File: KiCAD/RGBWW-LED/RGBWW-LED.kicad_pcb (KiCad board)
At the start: 2 copper layers, 0 parts

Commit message: added some library components and edited pdf
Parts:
- added C1: 1u, Capacitor_SMD:C_0603_1608Metric, F.Cu at (58.0, 82.9)
- added C10: 1u, Capacitor_SMD:C_0603_1608Metric, F.Cu at (58.0, 63.3)
- added C2: 1u, Capacitor_SMD:C_0603_1608Metric, F.Cu at (58.0, 85.4)
- added C3: 1u, Capacitor_SMD:C_0603_1608Metric, F.Cu at (90.6, 60.8)
- added C4: 1u, Capacitor_SMD:C_0603_1608Metric, F.Cu at (90.6, 63.3)
- added C5: 1u, Capacitor_SMD:C_0603_1608Metric, F.Cu at (90.6, 38.8)
- added C6: 1u, Capacitor_SMD:C_0603_1608Metric, F.Cu at (90.6, 41.3)
- added C7: 1u, Capacitor_SMD:C_0603_1608Metric, F.Cu at (58.0, 38.8)
- added C8: 1u, Capacitor_SMD:C_0603_1608Metric, F.Cu at (58.0, 41.3)
- added C9: 1u, Capacitor_SMD:C_0603_1608Metric, F.Cu at (58.0, 60.8)
- added J1: Conn_01x04, Connector_PinHeader_2.54mm:PinHeader_1x04_P2.54mm_Horizontal, F.Cu at (90.9, 84.0)
- added J2: Conn_01x04, Connector_PinHeader_2.54mm:PinHeader_1x04_P2.54mm_Horizontal, F.Cu at (90.9, 96.2)
- added R1: 4k7, Resistor_SMD:R_0603_1608Metric, F.Cu at (58.0, 87.9)
- added R10: 0R, Resistor_SMD:R_0603_1608Metric, F.Cu at (90.6, 73.4)
- added R11: 0R, Resistor_SMD:R_0603_1608Metric, F.Cu at (90.6, 75.9)
- added R12: 4k7, Resistor_SMD:R_0603_1608Metric, F.Cu at (90.6, 78.4)
- added R13: 0R, Resistor_SMD:R_0603_1608Metric, F.Cu at (90.6, 43.8)
- added R14: 0R, Resistor_SMD:R_0603_1608Metric, F.Cu at (90.6, 46.3)
- added R15: 0R, Resistor_SMD:R_0603_1608Metric, F.Cu at (90.6, 48.8)
- added R16: 0R, Resistor_SMD:R_0603_1608Metric, F.Cu at (90.6, 51.3)
- added R17: 0R, Resistor_SMD:R_0603_1608Metric, F.Cu at (90.6, 53.8)
- added R18: 4k7, Resistor_SMD:R_0603_1608Metric, F.Cu at (90.6, 56.3)
- added R19: 0R, Resistor_SMD:R_0603_1608Metric, F.Cu at (58.0, 43.8)
- added R2: 0R, Resistor_SMD:R_0603_1608Metric, F.Cu at (58.0, 90.4)
- added R20: 0R, Resistor_SMD:R_0603_1608Metric, F.Cu at (58.0, 46.3)
- added R21: 0R, Resistor_SMD:R_0603_1608Metric, F.Cu at (58.0, 48.8)
- added R22: 0R, Resistor_SMD:R_0603_1608Metric, F.Cu at (58.0, 51.3)
- added R23: 0R, Resistor_SMD:R_0603_1608Metric, F.Cu at (58.0, 53.8)
- added R24: 4k7, Resistor_SMD:R_0603_1608Metric, F.Cu at (58.0, 56.3)
- added R25: 0R, Resistor_SMD:R_0603_1608Metric, F.Cu at (58.0, 65.9)
- added R26: 0R, Resistor_SMD:R_0603_1608Metric, F.Cu at (58.0, 68.4)
- added R27: 0R, Resistor_SMD:R_0603_1608Metric, F.Cu at (58.0, 70.9)
- added R28: 0R, Resistor_SMD:R_0603_1608Metric, F.Cu at (58.0, 73.4)
- added R29: 0R, Resistor_SMD:R_0603_1608Metric, F.Cu at (58.0, 75.9)
- added R3: 0R, Resistor_SMD:R_0603_1608Metric, F.Cu at (58.0, 93.0)
- added R30: 4k7, Resistor_SMD:R_0603_1608Metric, F.Cu at (58.0, 78.4)
- added R31: 100R, Resistor_SMD:R_0603_1608Metric, F.Cu at (104.0, 82.9)
- added R32: 100R, Resistor_SMD:R_0603_1608Metric, F.Cu at (104.0, 85.4)
- added R4: 0R, Resistor_SMD:R_0603_1608Metric, F.Cu at (58.0, 95.5)
- added R5: 0R, Resistor_SMD:R_0603_1608Metric, F.Cu at (58.0, 98.0)
- added R6: 0R, Resistor_SMD:R_0603_1608Metric, F.Cu at (58.0, 100.5)
- added R7: 0R, Resistor_SMD:R_0603_1608Metric, F.Cu at (90.6, 65.9)
- added R8: 0R, Resistor_SMD:R_0603_1608Metric, F.Cu at (90.6, 68.4)
- added R9: 0R, Resistor_SMD:R_0603_1608Metric, F.Cu at (90.6, 70.9)
- added U1: H5050RGBWW-ZB-96427, LEDandDriver:LED_RGBWW_5050_10, F.Cu at (63.3, 82.4)
- added U10: H5050RGBWW-ZB-96427, LEDandDriver:LED_RGBWW_5050_10, F.Cu at (102.6, 38.2)
- added U11: H5050RGBWW-ZB-96427, LEDandDriver:LED_RGBWW_5050_10, F.Cu at (70.0, 38.2)
- added U12: WS2805, LEDandDriver:SOP-10-6mm-1mm, F.Cu at (109.2, 38.2)
- added U13: H5050RGBWW-ZB-96427, LEDandDriver:LED_RGBWW_5050_10, F.Cu at (70.0, 60.3)
- added U14: H5050RGBWW-ZB-96427, LEDandDriver:LED_RGBWW_5050_10, F.Cu at (83.3, 82.4)
- added U15: H5050RGBWW-ZB-96427, LEDandDriver:LED_RGBWW_5050_10, F.Cu at (115.9, 60.3)
- added U16: WS2805, LEDandDriver:SOP-10-6mm-1mm, F.Cu at (76.6, 38.2)
- added U17: H5050RGBWW-ZB-96427, LEDandDriver:LED_RGBWW_5050_10, F.Cu at (115.9, 38.2)
- added U18: H5050RGBWW-ZB-96427, LEDandDriver:LED_RGBWW_5050_10, F.Cu at (83.3, 38.2)
- added U19: H5050RGBWW-ZB-96427, LEDandDriver:LED_RGBWW_5050_10, F.Cu at (76.6, 60.3)
- added U2: H5050RGBWW-ZB-96427, LEDandDriver:LED_RGBWW_5050_10, F.Cu at (95.9, 60.3)
- added U20: WS2805, LEDandDriver:SOP-10-6mm-1mm, F.Cu at (83.3, 60.3)
- added U3: WS2805, LEDandDriver:SOP-10-6mm-1mm, F.Cu at (70.0, 82.4)
- added U4: H5050RGBWW-ZB-96427, LEDandDriver:LED_RGBWW_5050_10, F.Cu at (95.9, 38.2)
- added U5: H5050RGBWW-ZB-96427, LEDandDriver:LED_RGBWW_5050_10, F.Cu at (63.3, 38.2)
- added U6: H5050RGBWW-ZB-96427, LEDandDriver:LED_RGBWW_5050_10, F.Cu at (63.3, 60.3)
- added U7: H5050RGBWW-ZB-96427, LEDandDriver:LED_RGBWW_5050_10, F.Cu at (76.6, 82.4)
- added U8: WS2805, LEDandDriver:SOP-10-6mm-1mm, F.Cu at (102.6, 60.3)
- added U9: H5050RGBWW-ZB-96427, LEDandDriver:LED_RGBWW_5050_10, F.Cu at (109.2, 60.3)

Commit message: started layout, some mods to the lib
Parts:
- R10, R11, R13, R14, R15, R16, R17, R19, R2, R20, R21, R22, R23, R25, R26, R27, R28, R29, R3, R4, R5, R6, R7, R8, R9: value 0R -> 10R
- moved U12 123.5 mm to (45.1, 143.8)
- moved U3 112.2 mm to (153.1, 157.8)
- moved C2 110.4 mm to (140.8, 158.5)
- moved R1 110.4 mm to (140.8, 161.0)
- moved R2 110.4 mm to (140.8, 163.5)
- moved R3 110.4 mm to (140.8, 166.0)
- moved R4 110.4 mm to (140.8, 168.5)
- moved R5 110.4 mm to (140.8, 171.0)
- moved R6 110.4 mm to (140.8, 173.6)
- moved C1 110.4 mm to (140.8, 156.0)
- moved C8 108.7 mm to (119.5, 130.9), turned to -90 degrees
- moved C6 108.0 mm to (29.8, 130.5)
- moved R15 108.0 mm to (29.8, 138.0)
- moved R18 108.0 mm to (29.8, 145.6)
- moved C5 108.0 mm to (29.8, 128.0)
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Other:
- board outline added: 150 x 15 mm

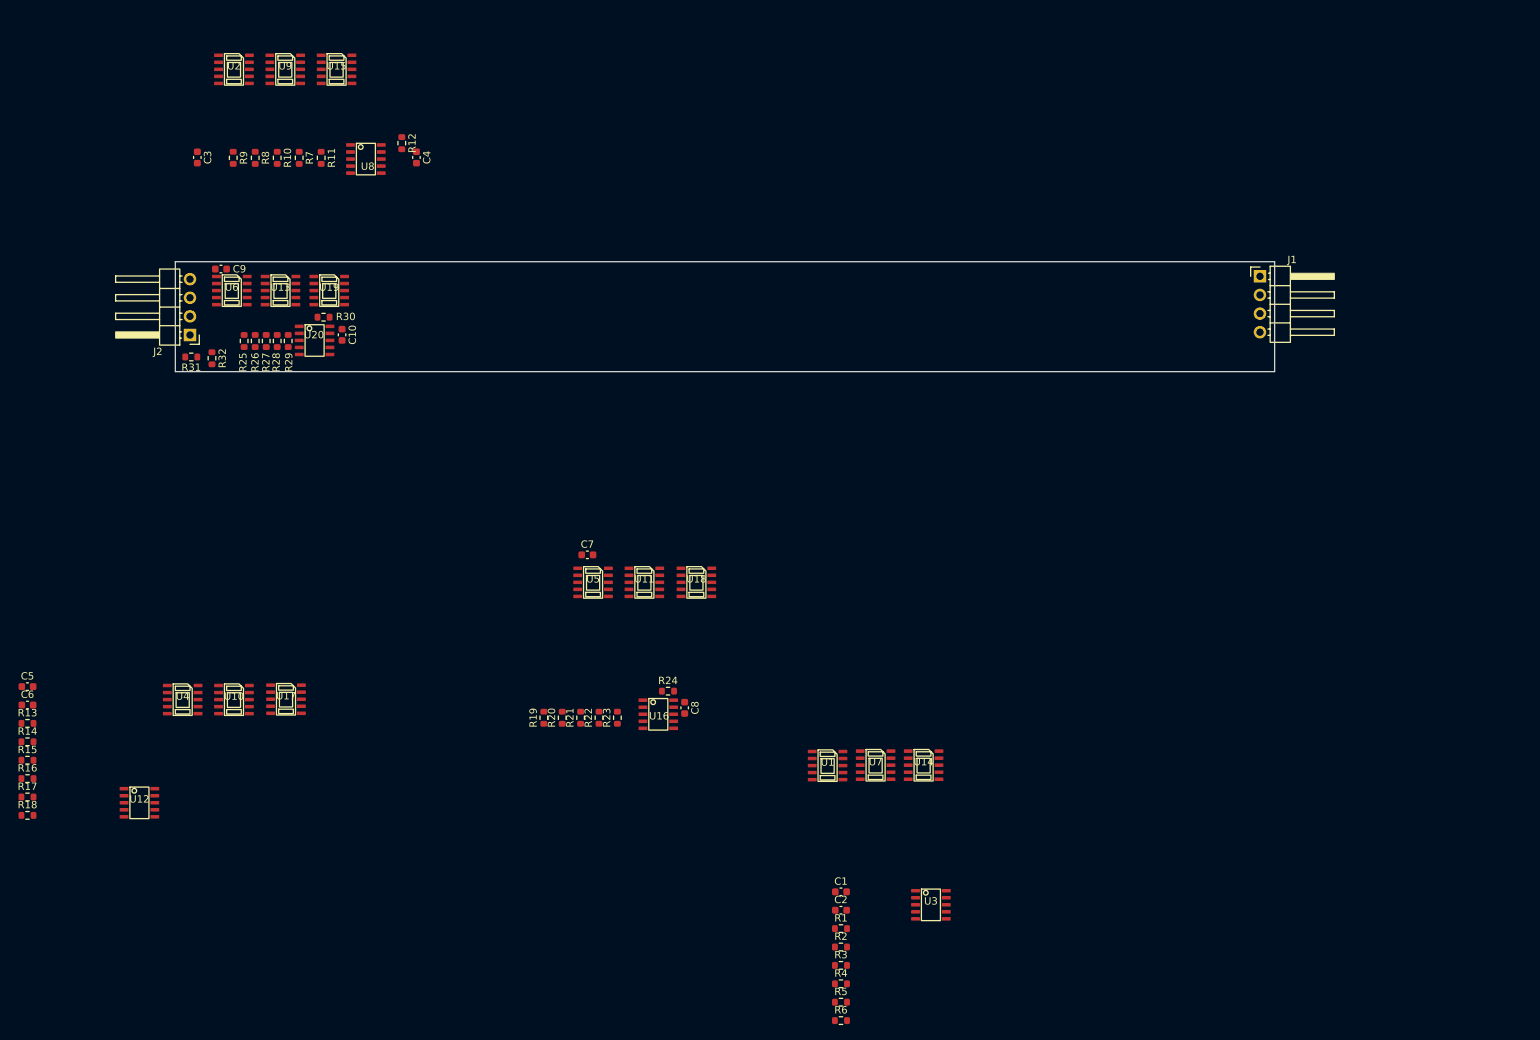
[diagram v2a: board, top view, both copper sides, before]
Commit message: added some datasheet and started controller
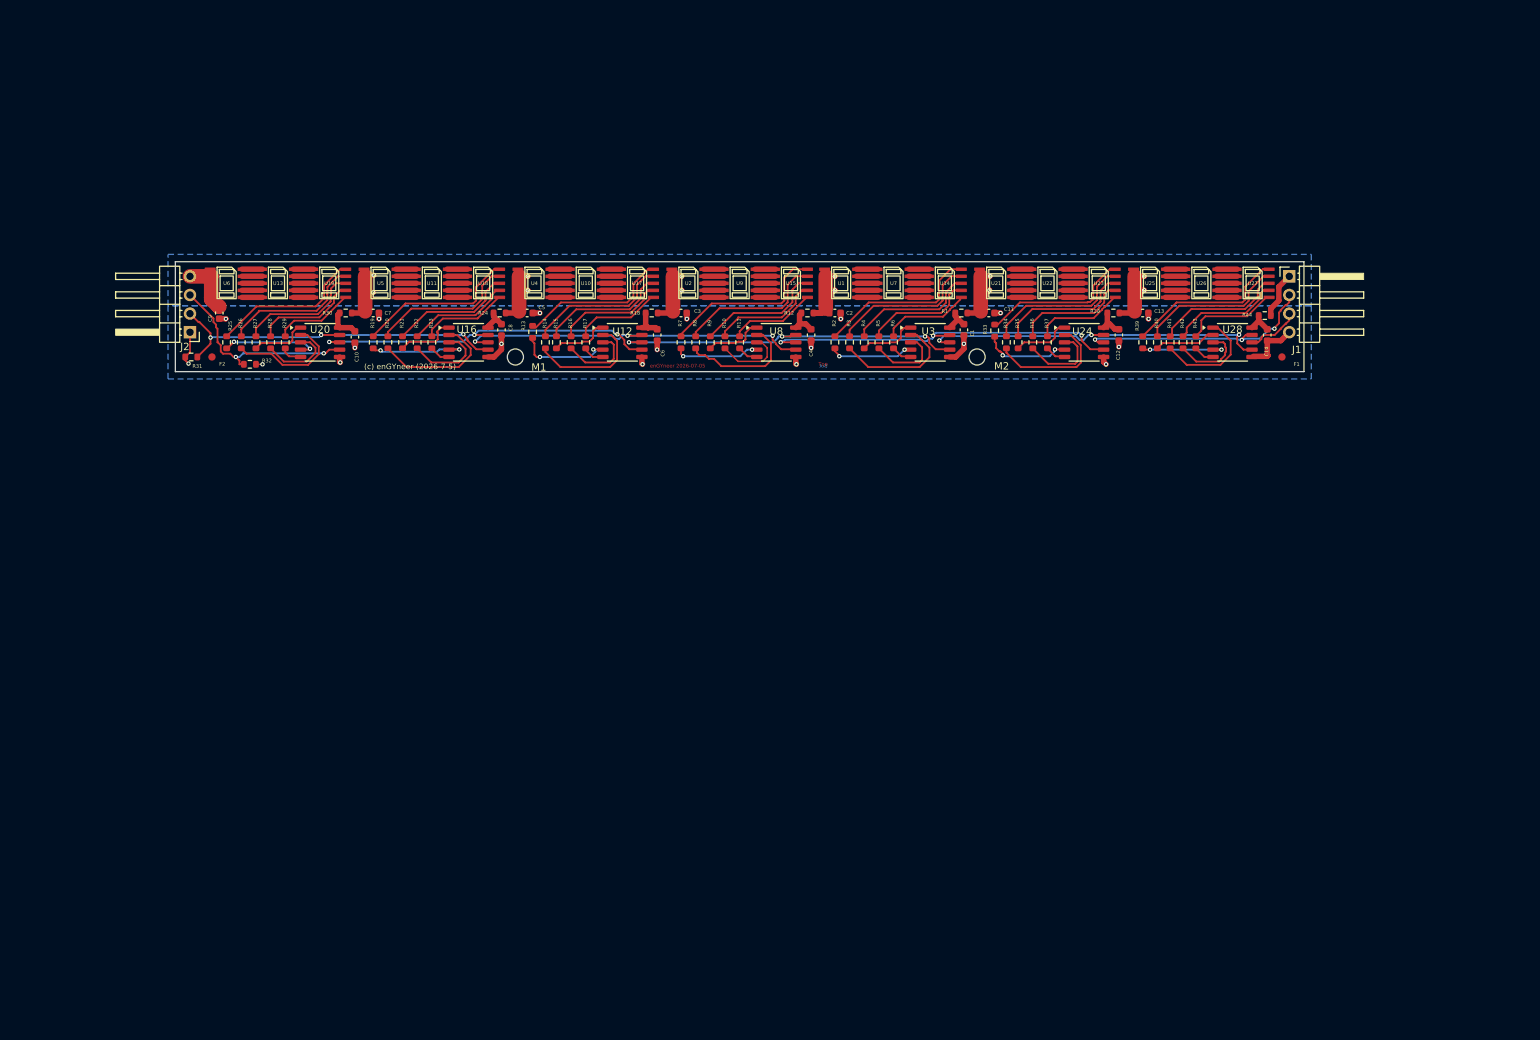
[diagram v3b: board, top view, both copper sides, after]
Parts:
- added C11: 1u, LEDandDriver:C_0603_1608Metric_LedPrj, F.Cu at (161.0, 77.0)
- added C12: 1u, LEDandDriver:C_0603_1608Metric_LedPrj, F.Cu at (178.8, 80.0)
- added C13: 1u, LEDandDriver:C_0603_1608Metric_LedPrj, F.Cu at (182.0, 77.0)
- added C14: 1u, LEDandDriver:C_0603_1608Metric_LedPrj, F.Cu at (199.0, 80.0)
- added F1: Fiducial, Fiducial:Fiducial_1mm_Mask2mm, F.Cu at (201.0, 83.0)
- added F2: Fiducial, Fiducial:Fiducial_1mm_Mask2mm, F.Cu at (55.0, 83.0)
- added M1: MountingHole, MountingHole:MountingHole_2.2mm_M2, F.Cu at (96.4, 83.0)
- added M2: MountingHole, MountingHole:MountingHole_2.2mm_M2, F.Cu at (159.4, 83.0)
- added R33: 10R, LEDandDriver:R_0603_1608Metric_LedPrj, F.Cu at (161.8, 79.4)
- added R34: 10R, LEDandDriver:R_0603_1608Metric_LedPrj, F.Cu at (163.4, 81.0)
- added R35: 10R, LEDandDriver:R_0603_1608Metric_LedPrj, F.Cu at (165.0, 81.0)
- added R36: 10R, LEDandDriver:R_0603_1608Metric_LedPrj, F.Cu at (167.0, 81.0)
- added R37: 10R, LEDandDriver:R_0603_1608Metric_LedPrj, F.Cu at (169.0, 81.0)
- added R38: 4k7, LEDandDriver:R_0603_1608Metric_LedPrj, F.Cu at (178.0, 77.0)
- added R39: 10R, LEDandDriver:R_0603_1608Metric_LedPrj, F.Cu at (182.0, 81.0)
- added R40: 10R, LEDandDriver:R_0603_1608Metric_LedPrj, F.Cu at (184.0, 81.0)
- added R41: 10R, LEDandDriver:R_0603_1608Metric_LedPrj, F.Cu at (185.8, 81.0)
- added R42: 10R, LEDandDriver:R_0603_1608Metric_LedPrj, F.Cu at (187.5, 81.0)
- added R43: 10R, LEDandDriver:R_0603_1608Metric_LedPrj, F.Cu at (189.2, 81.0)
- added R44: 4k7, LEDandDriver:R_0603_1608Metric_LedPrj, F.Cu at (198.7, 77.3)
- added U21: H5050RGBWW-ZB-96427, LEDandDriver:LED_RGBWW_5050_10, F.Cu at (162.0, 73.0)
- added U22: H5050RGBWW-ZB-96427, LEDandDriver:LED_RGBWW_5050_10, F.Cu at (169.0, 73.0)
- added U23: H5050RGBWW-ZB-96427, LEDandDriver:LED_RGBWW_5050_10, F.Cu at (176.0, 73.0)
- added U24: WS2805, Package_SO:SOIC-10_3.9x4.9mm_P1mm, F.Cu at (174.0, 81.0)
- added U25: H5050RGBWW-ZB-96427, LEDandDriver:LED_RGBWW_5050_10, F.Cu at (183.0, 73.0)
- added U26: H5050RGBWW-ZB-96427, LEDandDriver:LED_RGBWW_5050_10, F.Cu at (190.0, 73.0)
- added U27: H5050RGBWW-ZB-96427, LEDandDriver:LED_RGBWW_5050_10, F.Cu at (197.0, 73.0)
- added U28: WS2805, Package_SO:SOIC-10_3.9x4.9mm_P1mm, F.Cu at (194.2, 81.0)
- C1, C10, C2, C3, C4, C5, C6, C7, C8, C9: footprint Capacitor_SMD:C_0603_1608Metric -> LEDandDriver:C_0603_1608Metric_LedPrj
- R1, R10, R11, R12, R13, R14, R15, R16, R17, R18, R19, R2, R20, R21, R22, R23, R24, R25, R26, R27, R28, R29, R3, R30, R31, R32, R4, R5, R6, R7, R8, R9: footprint Resistor_SMD:R_0603_1608Metric -> LEDandDriver:R_0603_1608Metric_LedPrj
- U12, U16, U20, U3, U8: footprint LEDandDriver:SOP-10-6mm-1mm -> Package_SO:SOIC-10_3.9x4.9mm_P1mm
- moved R18 109.3 mm to (115.0, 77.0), turned to 180 degrees
- moved C6 99.7 mm to (115.8, 80.0), turned to -90 degrees
- moved R17 98.2 mm to (106.0, 81.0), turned to -90 degrees
- moved R16 95.1 mm to (104.0, 81.0), turned to -90 degrees
- moved R6 92.8 mm to (148.0, 81.0), turned to -90 degrees
- moved R15 92.0 mm to (102.0, 81.0), turned to -90 degrees
- moved U12 91.1 mm to (111.0, 81.0)
- moved R5 90.2 mm to (146.0, 81.0), turned to -90 degrees
- moved R14 89.3 mm to (100.5, 81.0), turned to -90 degrees
- moved R4 87.6 mm to (144.0, 81.0), turned to -90 degrees
- moved R13 87.2 mm to (98.8, 79.6), turned to -90 degrees
- moved R1 85.6 mm to (157.2, 77.0), turned to 180 degrees
- moved C5 85.1 mm to (98.0, 77.0)
- moved R3 85.0 mm to (142.0, 81.0), turned to -90 degrees
- moved R2 82.5 mm to (140.0, 81.0), turned to -90 degrees
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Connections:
- U3 pad 8: /Bin -> /LEDGruppe/Bin
- U3 pad 9: /Din -> /LEDGruppe/Din
- U8 pad 8: /Din -> /LEDGruppe/Din
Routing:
- net +12V: track 0.00 -> 72.2 mm, vias 0 -> 12
- net /LEDGruppe/Din: track 0.00 -> 48.9 mm, vias 0 -> 3
- net /Bout: track 0.00 -> 48.9 mm, vias 0 -> 3
- net /LEDGruppe1/Dout: track 0.00 -> 47.9 mm, vias 0 -> 3
- net /LEDGruppe/Bin: track 0.00 -> 47.4 mm, vias 0 -> 3
- net /LEDGruppe/Dout: track 0.00 -> 47.2 mm, vias 0 -> 3
- net /LEDGruppe2/Dout: track 0.00 -> 46.9 mm, vias 0 -> 3
- net GND: track 0.00 -> 35.3 mm, vias 0 -> 19
- net /Din: track 0.00 -> 33.5 mm, vias 0 -> 3
- net /Dout: track 0.00 -> 28.2 mm, vias 0 -> 2
- net Net-(U15-W1-C): track 0.00 -> 22.9 mm
- net Net-(U14-W1-C): track 0.00 -> 22.4 mm
- net Net-(U18-W1-C): track 0.00 -> 22.0 mm
- net Net-(U27-W1-C): track 0.00 -> 21.9 mm
- net Net-(U19-W1-C): track 0.00 -> 21.0 mm
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- added copper zone on B.Cu, net +12V
- added copper zone on B.Cu, net GND
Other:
- board size 150 x 15 mm -> 154 x 15 mm
- board text added: "(c) enGYneer (2026-7-5)"
- board text added: "Bot"
- board text added: "Top"
- board text added: "enGYneer 2026-07-05"

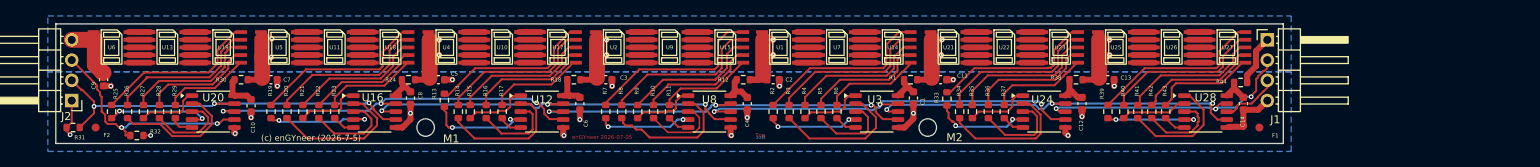
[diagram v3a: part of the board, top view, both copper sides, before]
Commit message: longer LED board
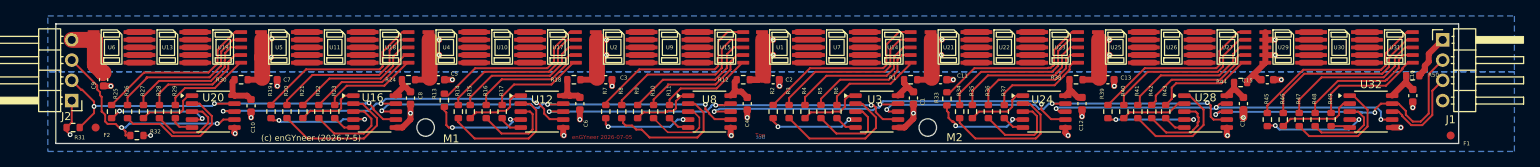
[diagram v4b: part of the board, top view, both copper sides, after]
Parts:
- added C15: 1u, LEDandDriver:C_0603_1608Metric_LedPrj, F.Cu at (202.0, 77.0)
- added C16: 1u, LEDandDriver:C_0603_1608Metric_LedPrj, F.Cu at (220.2, 79.0)
- added R45: 10R, LEDandDriver:R_0603_1608Metric_LedPrj, F.Cu at (202.0, 82.0)
- added R46: 10R, LEDandDriver:R_0603_1608Metric_LedPrj, F.Cu at (204.0, 82.0)
- added R47: 10R, LEDandDriver:R_0603_1608Metric_LedPrj, F.Cu at (206.0, 82.0)
- added R48: 10R, LEDandDriver:R_0603_1608Metric_LedPrj, F.Cu at (208.0, 82.0)
- added R49: 10R, LEDandDriver:R_0603_1608Metric_LedPrj, F.Cu at (210.0, 82.0)
- added R50: 4k7, LEDandDriver:R_0603_1608Metric_LedPrj, F.Cu at (220.2, 76.5)
- added U29: H5050RGBWW-ZB-96427, LEDandDriver:LED_RGBWW_5050_10, F.Cu at (204.0, 73.0)
- added U30: H5050RGBWW-ZB-96427, LEDandDriver:LED_RGBWW_5050_10, F.Cu at (211.0, 73.0)
- added U31: H5050RGBWW-ZB-96427, LEDandDriver:LED_RGBWW_5050_10, F.Cu at (218.0, 73.0)
- added U32: WS2805, Package_SO:SOIC-10_3.9x4.9mm_P1mm, F.Cu at (215.0, 81.0)
- moved F1 24.0 mm to (225.0, 84.0)
- moved J1 22.0 mm to (224.0, 72.0)
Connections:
- U24 pad 8: /Din -> /LEDGruppe5/Bin
- U28 pad 8: /Bin -> /Din
- U28 pad 9: /Din -> /LEDGruppe5/Bin
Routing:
- net /LEDGruppe5/Bin: track 0.00 -> 46.1 mm, vias 0 -> 3
- net Net-(U31-W1-C): track 0.00 -> 23.9 mm
- net Net-(U31-G-C): track 0.00 -> 22.1 mm
- net Net-(U31-R-C): track 0.00 -> 19.3 mm
- net Net-(U31-B-C): track 0.00 -> 16.5 mm
- net Net-(U32-OutR): track 0.00 -> 14.7 mm
- net Net-(U31-W2-C): track 0.00 -> 14.4 mm
- net Net-(U32-OutW1): track 0.00 -> 13.4 mm, vias 0 -> 2
- net +12V: track 72.2 -> 82.5 mm, vias 12 -> 14
- net Net-(U32-OutG): track 0.00 -> 10.3 mm
- net Net-(U32-OutB): track 0.00 -> 9.88 mm
- net /Din: track 33.5 -> 38.2 mm, vias 3 -> 2
- net Net-(U32-Vdd): track 0.00 -> 4.49 mm
- net /Bin: track 7.22 -> 11.2 mm
- net GND: track 35.3 -> 32.5 mm, vias 19 -> 24
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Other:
- board size 154 x 15 mm -> 176 x 15 mm
